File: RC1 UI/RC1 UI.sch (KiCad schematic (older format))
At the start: 56 parts, among them J1 KB, J2 RC1_UI_Port, J3 COM, M1 Mounting, M2 Mounting, M3 Mounting, M4 Mounting, Q1 2N3906, Q2 2N3906, Q3 2N3906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

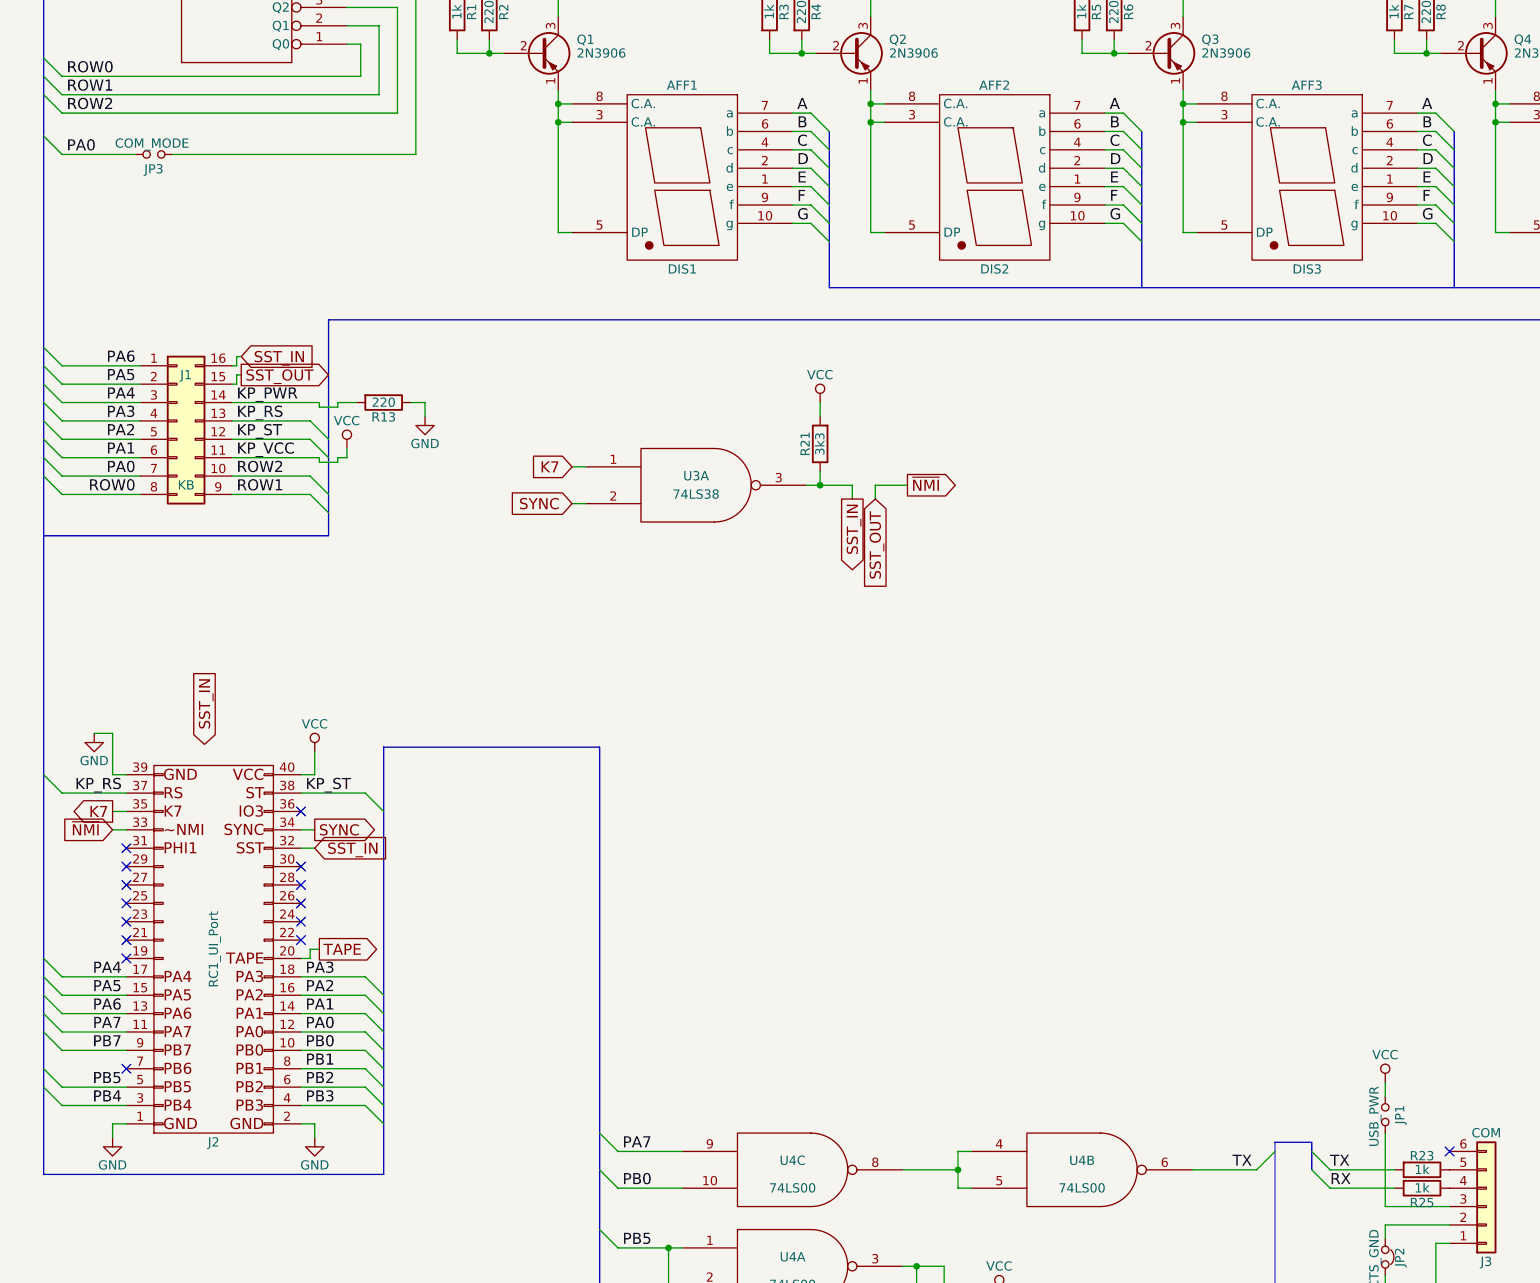
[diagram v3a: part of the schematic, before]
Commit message: UI layout done
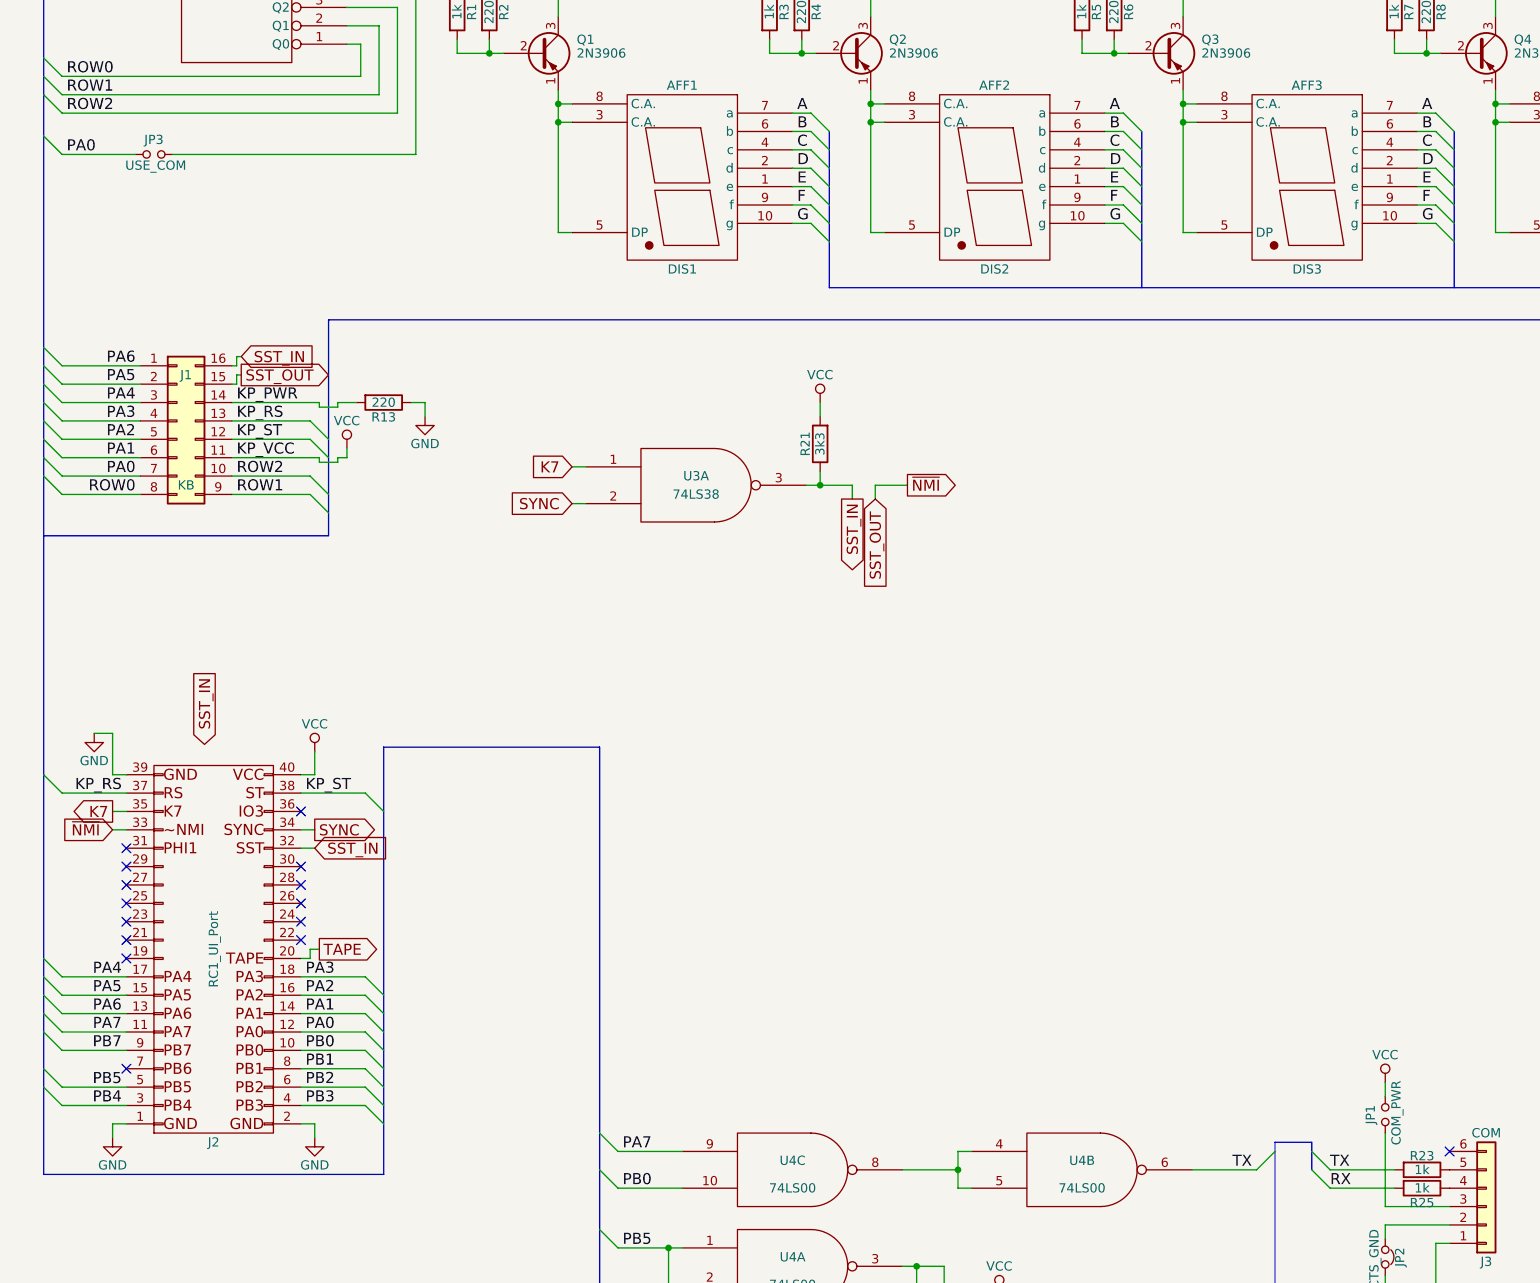
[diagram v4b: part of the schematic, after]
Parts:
- JP1: value USB_PWR -> COM_PWR
- JP3: value COM_MODE -> USE_COM
- R13, R14, R15, R16, R17, R18, R19, R20, R21, R22, R23, R24, R25, R26: footprint Resistors_THT:R_Axial_DIN0207_L6.3mm_D2.5mm_P5.08mm_Vertical -> Resistors_THT:R_Axial_DIN0207_L6.3mm_D2.5mm_P10.16mm_Horizontal
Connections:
- net PA0: now also JP3.1; no longer JP3.2
- net VCC: now also JP1.2; no longer JP1.1
- net at U1.4 (Q3): now also JP3.2; no longer JP3.1
- net at J3.3 (Pin_3): now also JP1.1; no longer JP1.2
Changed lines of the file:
@@
 F 0 "R13" V 3455 3825 50  0000 C CNN
 F 1 "220" V 3375 3825 50  0000 C CNN
-F 2 "Resistors_THT:R_Axial_DIN0207_L6.3mm_D2.5mm_P5.08mm_Vertical" V 3305 3825 50  0001 C CNN
+F 2 "Resistors_THT:R_Axial_DIN0207_L6.3mm_D2.5mm_P10.16mm_Horizontal" V 3305 3825 50  0001 C CNN
 F 3 "" H 3375 3825 50  0001 C CNN
 	1    3375 3825
@@
 F 0 "R14" V 14505 4025 50  0000 C CNN
 F 1 "82" V 14425 4025 50  0000 C CNN
-F 2 "Resistors_THT:R_Axial_DIN0207_L6.3mm_D2.5mm_P5.08mm_Vertical" V 14355 4025 50  0001 C CNN
+F 2 "Resistors_THT:R_Axial_DIN0207_L6.3mm_D2.5mm_P10.16mm_Horizontal" V 14355 4025 50  0001 C CNN
 F 3 "" H 14425 4025 50  0001 C CNN
 	1    14425 4025
@@
 F 0 "R15" V 14505 4400 50  0000 C CNN
 F 1 "82" V 14425 4400 50  0000 C CNN
-F 2 "Resistors_THT:R_Axial_DIN0207_L6.3mm_D2.5mm_P5.08mm_Vertical" V 14355 4400 50  0001 C CNN
+F 2 "Resistors_THT:R_Axial_DIN0207_L6.3mm_D2.5mm_P10.16mm_Horizontal" V 14355 4400 50  0001 C CNN
 F 3 "" H 14425 4400 50  0001 C CNN
 	1    14425 4400
@@
 F 0 "R16" V 14505 4775 50  0000 C CNN
 F 1 "82" V 14425 4775 50  0000 C CNN
-F 2 "Resistors_THT:R_Axial_DIN0207_L6.3mm_D2.5mm_P5.08mm_Vertical" V 14355 4775 50  0001 C CNN
+F 2 "Resistors_THT:R_Axial_DIN0207_L6.3mm_D2.5mm_P10.16mm_Horizontal" V 14355 4775 50  0001 C CNN
 F 3 "" H 14425 4775 50  0001 C CNN
 	1    14425 4775
@@
 F 0 "R17" V 14505 5425 50  0000 C CNN
 F 1 "82" V 14425 5425 50  0000 C CNN
-F 2 "Resistors_THT:R_Axial_DIN0207_L6.3mm_D2.5mm_P5.08mm_Vertical" V 14355 5425 50  0001 C CNN
+F 2 "Resistors_THT:R_Axial_DIN0207_L6.3mm_D2.5mm_P10.16mm_Horizontal" V 14355 5425 50  0001 C CNN
 F 3 "" H 14425 5425 50  0001 C CNN
 	1    14425 5425
@@
 F 0 "R18" V 14505 5900 50  0000 C CNN
 F 1 "82" V 14425 5900 50  0000 C CNN
-F 2 "Resistors_THT:R_Axial_DIN0207_L6.3mm_D2.5mm_P5.08mm_Vertical" V 14355 5900 50  0001 C CNN
+F 2 "Resistors_THT:R_Axial_DIN0207_L6.3mm_D2.5mm_P10.16mm_Horizontal" V 14355 5900 50  0001 C CNN
 F 3 "" H 14425 5900 50  0001 C CNN
 	1    14425 5900
@@
 F 0 "R19" V 14505 6275 50  0000 C CNN
 F 1 "82" V 14425 6275 50  0000 C CNN
-F 2 "Resistors_THT:R_Axial_DIN0207_L6.3mm_D2.5mm_P5.08mm_Vertical" V 14355 6275 50  0001 C CNN
+F 2 "Resistors_THT:R_Axial_DIN0207_L6.3mm_D2.5mm_P10.16mm_Horizontal" V 14355 6275 50  0001 C CNN
 F 3 "" H 14425 6275 50  0001 C CNN
 	1    14425 6275
@@
 F 0 "R20" V 14505 6650 50  0000 C CNN
 F 1 "82" V 14425 6650 50  0000 C CNN
-F 2 "Resistors_THT:R_Axial_DIN0207_L6.3mm_D2.5mm_P5.08mm_Vertical" V 14355 6650 50  0001 C CNN
+F 2 "Resistors_THT:R_Axial_DIN0207_L6.3mm_D2.5mm_P10.16mm_Horizontal" V 14355 6650 50  0001 C CNN
 F 3 "" H 14425 6650 50  0001 C CNN
 	1    14425 6650
@@
 F 0 "R21" V 5830 4050 50  0000 C CNN
 F 1 "3k3" V 5750 4050 50  0000 C CNN
-F 2 "Resistors_THT:R_Axial_DIN0207_L6.3mm_D2.5mm_P5.08mm_Vertical" V 5680 4050 50  0001 C CNN
+F 2 "Resistors_THT:R_Axial_DIN0207_L6.3mm_D2.5mm_P10.16mm_Horizontal" V 5680 4050 50  0001 C CNN
 F 3 "" H 5750 4050 50  0001 C CNN
 	1    5750 4050
@@
 F 0 "R22" V 6130 9975 50  0000 C CNN
 F 1 "1k" V 6050 9975 50  0000 C CNN
-F 2 "Resistors_THT:R_Axial_DIN0207_L6.3mm_D2.5mm_P5.08mm_Vertical" V 5980 9975 50  0001 C CNN
+F 2 "Resistors_THT:R_Axial_DIN0207_L6.3mm_D2.5mm_P10.16mm_Horizontal" V 5980 9975 50  0001 C CNN
 F 3 "" H 6050 9975 50  0001 C CNN
 	1    6050 9975
@@
 F 0 "R24" V 6805 8900 50  0000 C CNN
 F 1 "1k" V 6725 8900 50  0000 C CNN
-F 2 "Resistors_THT:R_Axial_DIN0207_L6.3mm_D2.5mm_P5.08mm_Vertical" V 6655 8900 50  0001 C CNN
+F 2 "Resistors_THT:R_Axial_DIN0207_L6.3mm_D2.5mm_P10.16mm_Horizontal" V 6655 8900 50  0001 C CNN
 F 3 "" H 6725 8900 50  0001 C CNN
 	1    6725 8900
@@
 F 0 "R26" V 10405 9450 50  0000 C CNN
 F 1 "1k" V 10325 9450 50  0000 C CNN
-F 2 "Resistors_THT:R_Axial_DIN0207_L6.3mm_D2.5mm_P5.08mm_Vertical" V 10255 9450 50  0001 C CNN
+F 2 "Resistors_THT:R_Axial_DIN0207_L6.3mm_D2.5mm_P10.16mm_Horizontal" V 10255 9450 50  0001 C CNN
 F 3 "" H 10325 9450 50  0001 C CNN
 	1    10325 9450
@@
 P 8825 7700
 F 0 "JP1" H 8825 7780 50  0000 C CNN
-F 1 "USB_PWR" H 8835 7640 50  0000 C CNN
+F 1 "COM_PWR" H 8835 7640 50  0000 C CNN
 F 2 "Pin_Headers:Pin_Header_Straight_1x02_Pitch2.54mm" H 8825 7700 50  0001 C CNN
 F 3 "" H 8825 7700 50  0001 C CNN
 	1    8825 7700
-	0    1    1    0
+	0    -1   -1   0
 $EndComp
 NoConn ~ 9175 7900
@@
 F 0 "R23" V 8950 8000 50  0000 C CNN
 F 1 "1k" V 9025 8000 50  0000 C CNN
-F 2 "Resistors_THT:R_Axial_DIN0207_L6.3mm_D2.5mm_P5.08mm_Vertical" V 8955 8000 50  0001 C CNN
+F 2 "Resistors_THT:R_Axial_DIN0207_L6.3mm_D2.5mm_P10.16mm_Horizontal" V 8955 8000 50  0001 C CNN
 F 3 "" H 9025 8000 50  0001 C CNN
 	1    9025 8000
@@
 F 0 "R25" V 9105 8100 50  0000 C CNN
 F 1 "1k" V 9025 8100 50  0000 C CNN
-F 2 "Resistors_THT:R_Axial_DIN0207_L6.3mm_D2.5mm_P5.08mm_Vertical" V 8955 8100 50  0001 C CNN
+F 2 "Resistors_THT:R_Axial_DIN0207_L6.3mm_D2.5mm_P10.16mm_Horizontal" V 8955 8100 50  0001 C CNN
 F 3 "" H 9025 8100 50  0001 C CNN
 	1    9025 8100
@@
 P 2125 2475
 F 0 "JP3" H 2125 2555 50  0000 C CNN
-F 1 "COM_MODE" H 2135 2415 50  0000 C CNN
+F 1 "USE_COM" H 2135 2415 50  0000 C CNN
 F 2 "Pin_Headers:Pin_Header_Straight_1x02_Pitch2.54mm" H 2125 2475 50  0001 C CNN
 F 3 "" H 2125 2475 50  0001 C CNN
 	1    2125 2475
-	-1   0    0    1
+	1    0    0    -1
 $EndComp
 Text GLabel 2400 5300 3    60   Output ~ 0
